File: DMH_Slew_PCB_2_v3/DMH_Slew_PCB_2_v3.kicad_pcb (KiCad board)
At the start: 2 copper layers, 48 x 141 mm, 22 parts, among them J50 Conn_01x08_PinHeader, J51 Conn_01x08_PinHeader, J60 Conn_01x08_PinHeader, J61 Conn_01x08_PinHeader, SW1 SW_DPDT_3way, SW2 SW_DPDT, SW3 SPDT_OnOffOn, SW4 SW_DPDT_3way, SW5 SW_DPDT, SW6 SPDT_OnOffOn

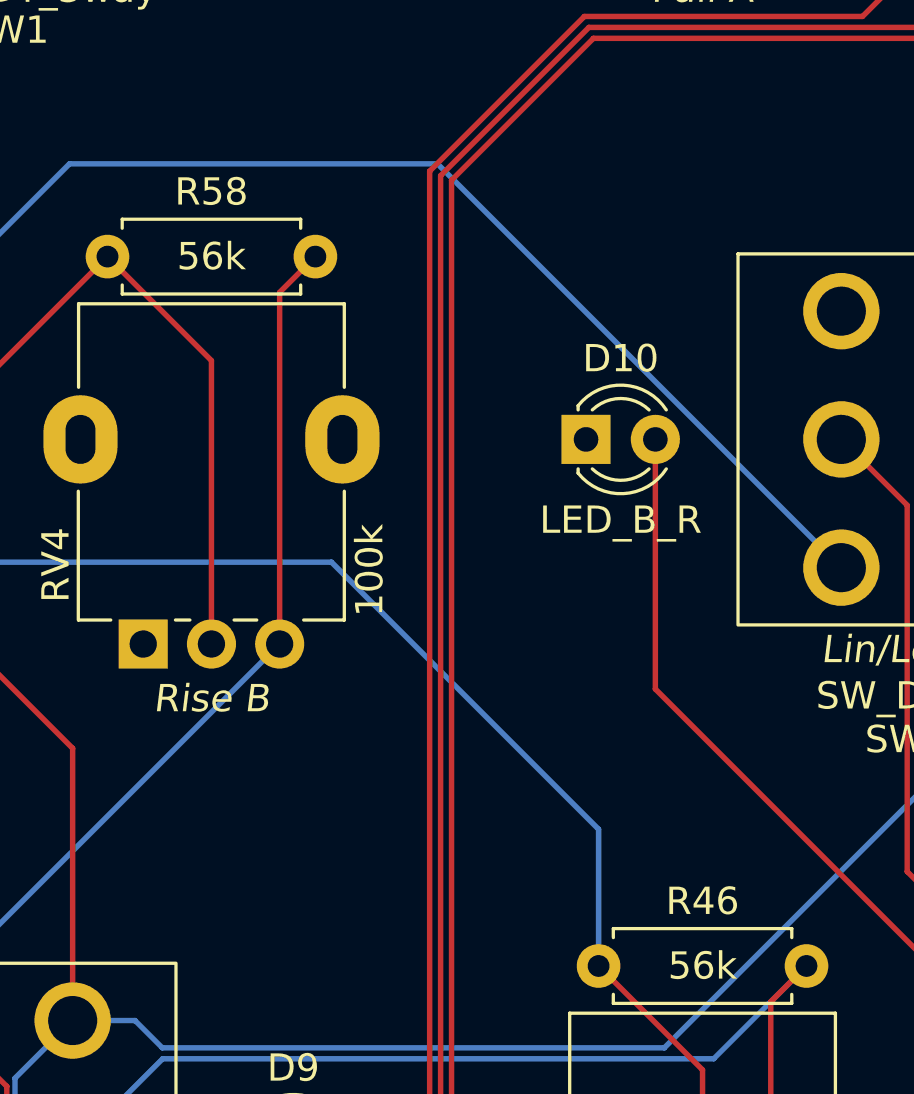
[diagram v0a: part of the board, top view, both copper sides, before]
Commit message: Relinked PCB1 and 2 with new v3 schematics
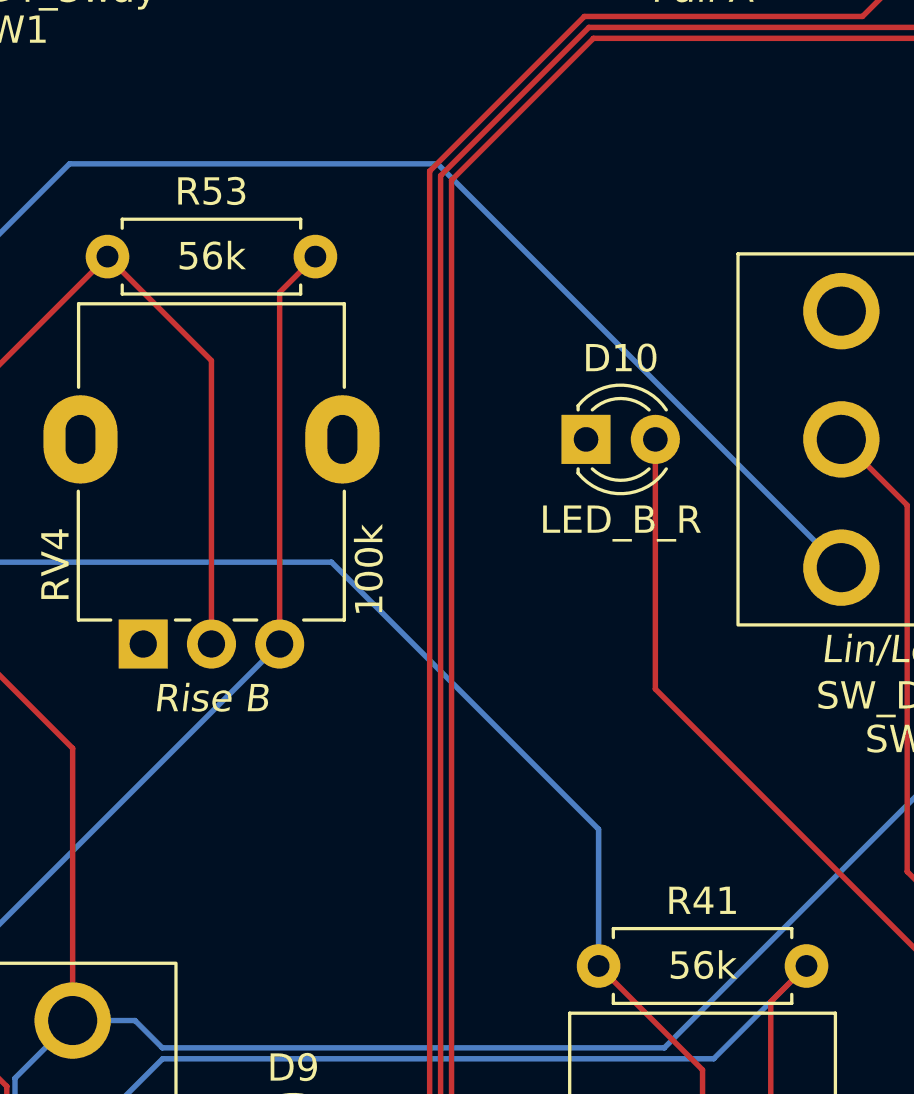
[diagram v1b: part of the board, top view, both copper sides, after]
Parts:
- J19: renamed from J50; value Conn_01x08_PinHeader -> Conn_01x08
- J20: renamed from J51; value Conn_01x08_PinHeader -> Conn_01x08
- J29: renamed from J60; value Conn_01x08_PinHeader -> Conn_01x08
- J30: renamed from J61; value Conn_01x08_PinHeader -> Conn_01x08
- renumbered R46 to R41, R58 to R53
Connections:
- net /Core Circuit A/Fall_CV renamed A_Fall_CV_C
- net /Core Circuit A/Output renamed A_Out_Jack_C
- net /Core Circuit A/Rise_CV renamed A_Rise_CV_C
- net /Core Circuit B/Fall_CV renamed B_Fall_CV_C
- net /Core Circuit B/Output renamed B_Out_Jack_C
- net /Core Circuit B/Rise_CV renamed B_Rise_CV_C
- net Net-(D10-A) renamed B_R_LED_C
- net Net-(D5-A) renamed A_F_LED_C
- net Net-(D6-A) renamed A_R_LED_C
- net Net-(D9-A) renamed B_F_LED_C
- net Net-(J50B-Pin_2) renamed A_Diff_Amp_C
- net Net-(J50F-Pin_6) renamed A_CV_Buff_C
- net Net-(J51A-Pin_1) renamed A_LinLog_Sw_p5_C
- net Net-(J51B-Pin_2) renamed A_LinLog_Sw_p2_C
- net Net-(J51E-Pin_5) renamed A_Rng_Sw_p3_C
- net Net-(J51G-Pin_7) renamed A_Rng_Sw_p1_C
- net Net-(J60B-Pin_2) renamed B_Diff_Amp_C
- net Net-(J60F-Pin_6) renamed B_CV_Buff_C
- net Net-(J61A-Pin_1) renamed B_LinLog_Sw_p5_C
- net Net-(J61B-Pin_2) renamed B_LinLog_Sw_p2_C
- net Net-(J61E-Pin_5) renamed B_Rng_Sw_p3_C
- net Net-(J61G-Pin_7) renamed B_Rng_Sw_p1_C

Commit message: Generated Gerbers
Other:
- board text added: "Mk1.0 - March 2026"
- board text removed: "Mk1.0 - Month Year"
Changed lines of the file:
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@@
 			(plot_on_all_layers_selection 0x00000000_00000000_00000000_00000000)
 			(disableapertmacros no)
-			(usegerberextensions no)
+			(usegerberextensions yes)
 			(usegerberattributes yes)
 			(usegerberadvancedattributes yes)
@@
 			(sketchdnponfab yes)
 			(crossoutdnponfab yes)
-			(subtractmaskfromsilk no)
+			(subtractmaskfromsilk yes)
 			(outputformat 1)
 			(mirror no)
-			(drillshape 1)
+			(drillshape 0)
 			(scaleselection 1)
-			(outputdirectory "")
+			(outputdirectory "Gerbers/")
 		)
 	)
@@
 		(layer "User.9")
 	)
-	(gr_text "Mk1.0 - Month Year"
+	(gr_text "Mk1.0 - March 2026"
 		(at 82.25 149.4 0)
 		(layer "B.SilkS")

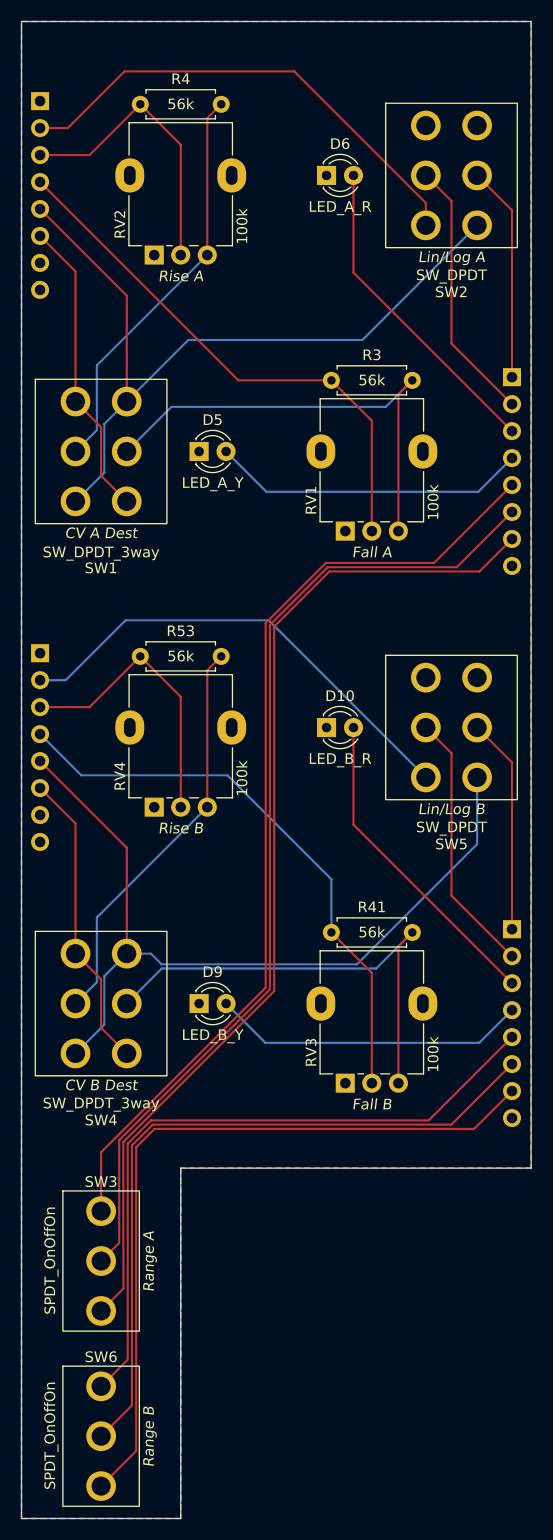
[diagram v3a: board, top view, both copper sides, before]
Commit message: Corrected PCB 2 switch positions
and Regenerated Gerbers
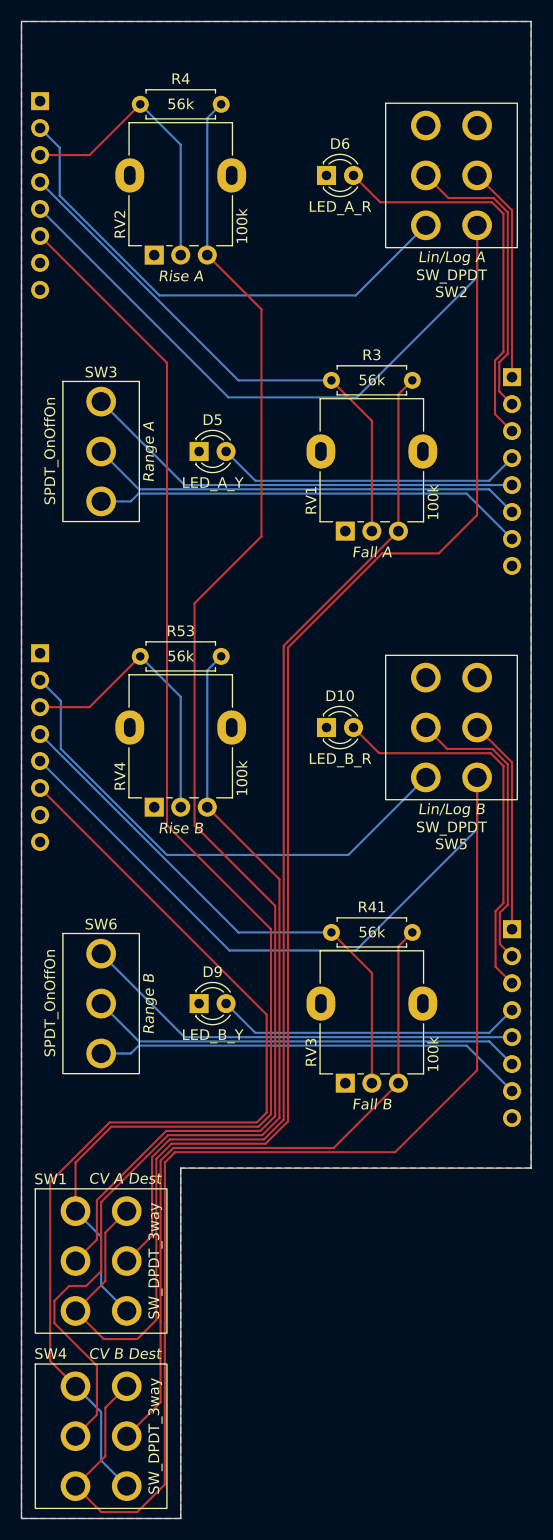
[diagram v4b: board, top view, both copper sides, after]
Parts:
- moved SW1 76.2 mm to (58.5, 159.2)
- moved SW3 76.2 mm to (58.5, 83.0)
- moved SW4 40.8 mm to (58.5, 175.8)
- moved SW6 40.8 mm to (58.5, 135.0)
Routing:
- net +10V_A: track 72.8 -> 202.9 mm
- net A_CV_Buff_C: track 28.4 -> 128.0 mm
- net +10V_B: track 77.3 -> 171.0 mm
- net Net-(R4-Pad2): track 38.4 -> 130.3 mm
- net B_CV_Buff_C: track 28.4 -> 94.1 mm
- net A_Rng_Sw_p1_C: track 97.0 -> 40.8 mm
- net Net-(R53-Pad2): track 38.4 -> 94.2 mm
- net Net-(R3-Pad2): track 44.4 -> 99.3 mm
- net A_Out_Jack_C: track 93.7 -> 41.1 mm
- net A_Rng_Sw_p3_C: track 90.4 -> 42.0 mm
- net B_Rng_Sw_p1_C: track 70.9 -> 40.8 mm
- net B_Out_Jack_C: track 67.6 -> 41.1 mm
- net Net-(R41-Pad2): track 44.4 -> 67.4 mm
- net B_Rng_Sw_p3_C: track 64.2 -> 42.0 mm
- net A_R_LED_C: track 30.3 -> 37.1 mm
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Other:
- board text added: "Mk1.1 - April 2026"
- board text removed: "Mk1.0 - March 2026"

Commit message: Redesigned Main PCB
and regenerated Gerbers
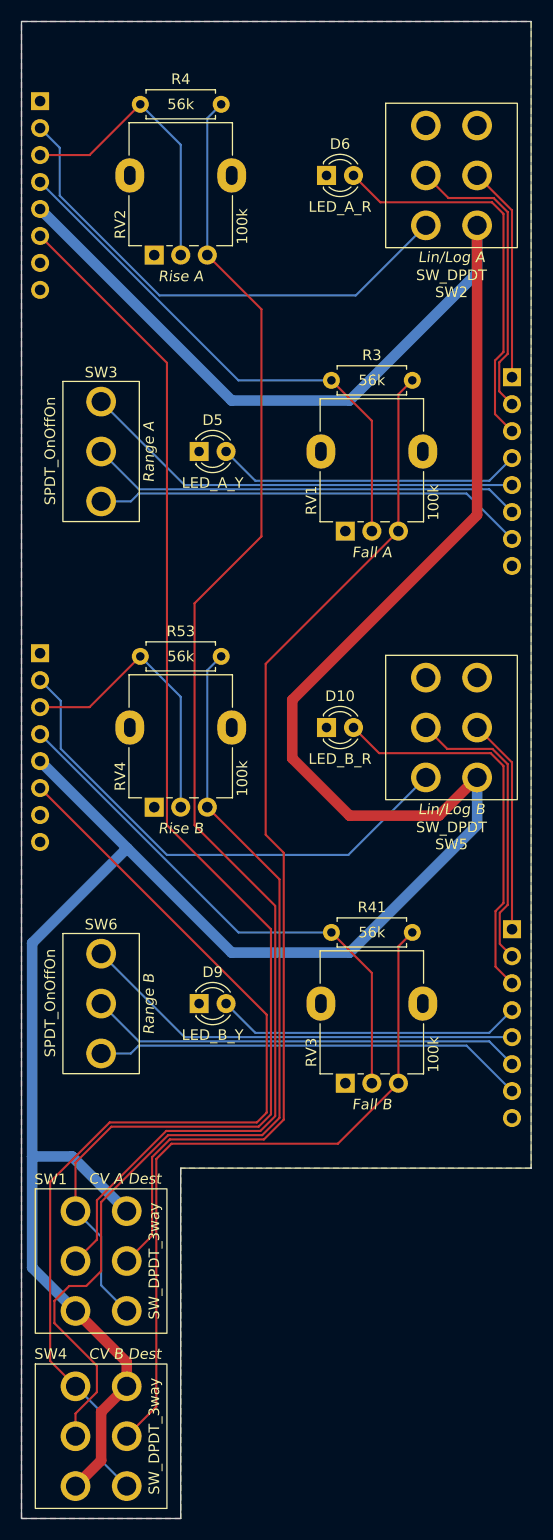
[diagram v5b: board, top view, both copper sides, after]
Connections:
- J19 pad 5: +10V_A -> +10V
- J29 pad 5: +10V_B -> +10V
- SW1 pad 1: +10V_A -> +10V
- SW1 pad 6: +10V_A -> +10V
- SW2 pad 4: +10V_A -> +10V
- SW4 pad 1: +10V_B -> +10V
- SW4 pad 6: +10V_B -> +10V
- SW5 pad 4: +10V_B -> +10V
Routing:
- net +10V: track 0.00 -> 275.3 mm
- net +10V_A: track 202.9 -> 0.00 mm
- net +10V_B: track 171.0 -> 0.00 mm
- net Net-(R3-Pad2): track 99.3 -> 100.7 mm
